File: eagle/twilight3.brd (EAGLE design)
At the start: 58 x 22 mm, 19 parts, among them IC1 TINY85, IC2 7805TV, Q1 IRF540

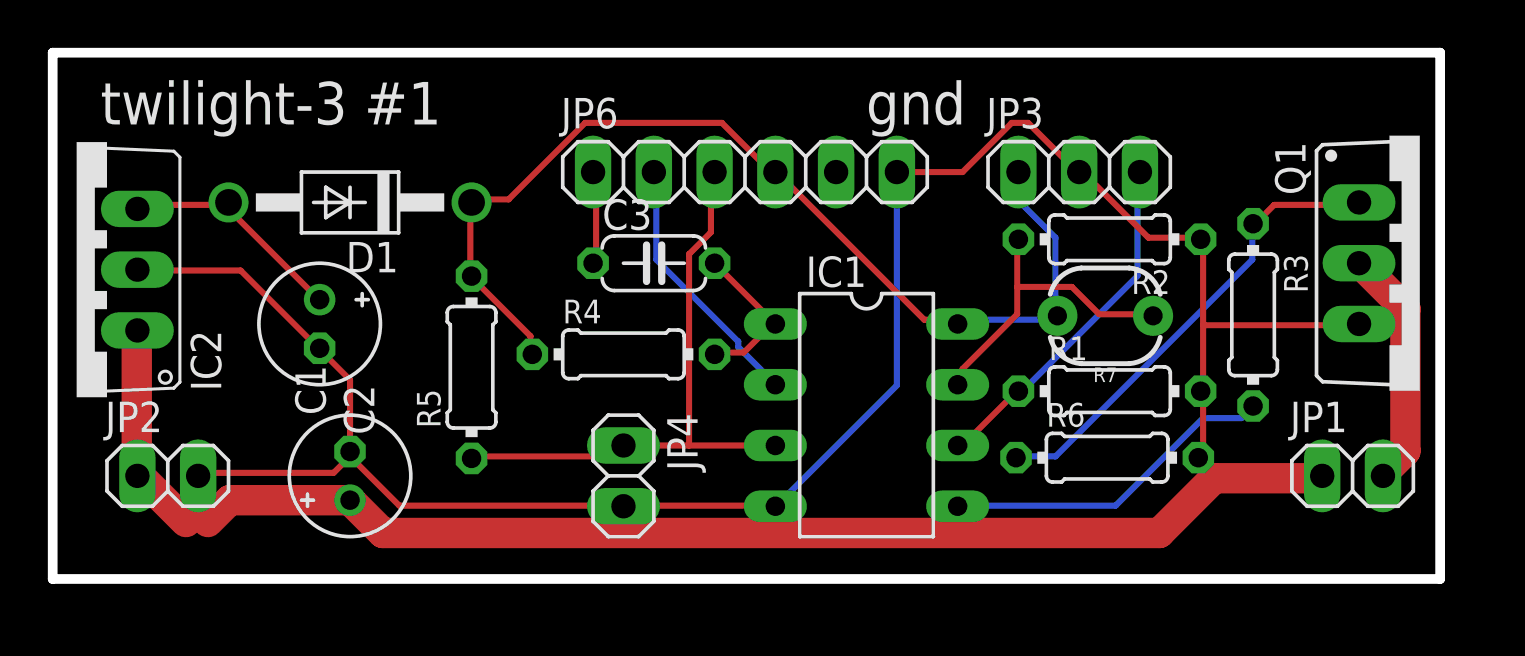
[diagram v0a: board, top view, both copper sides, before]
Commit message: fix issues #2, #3 and #4
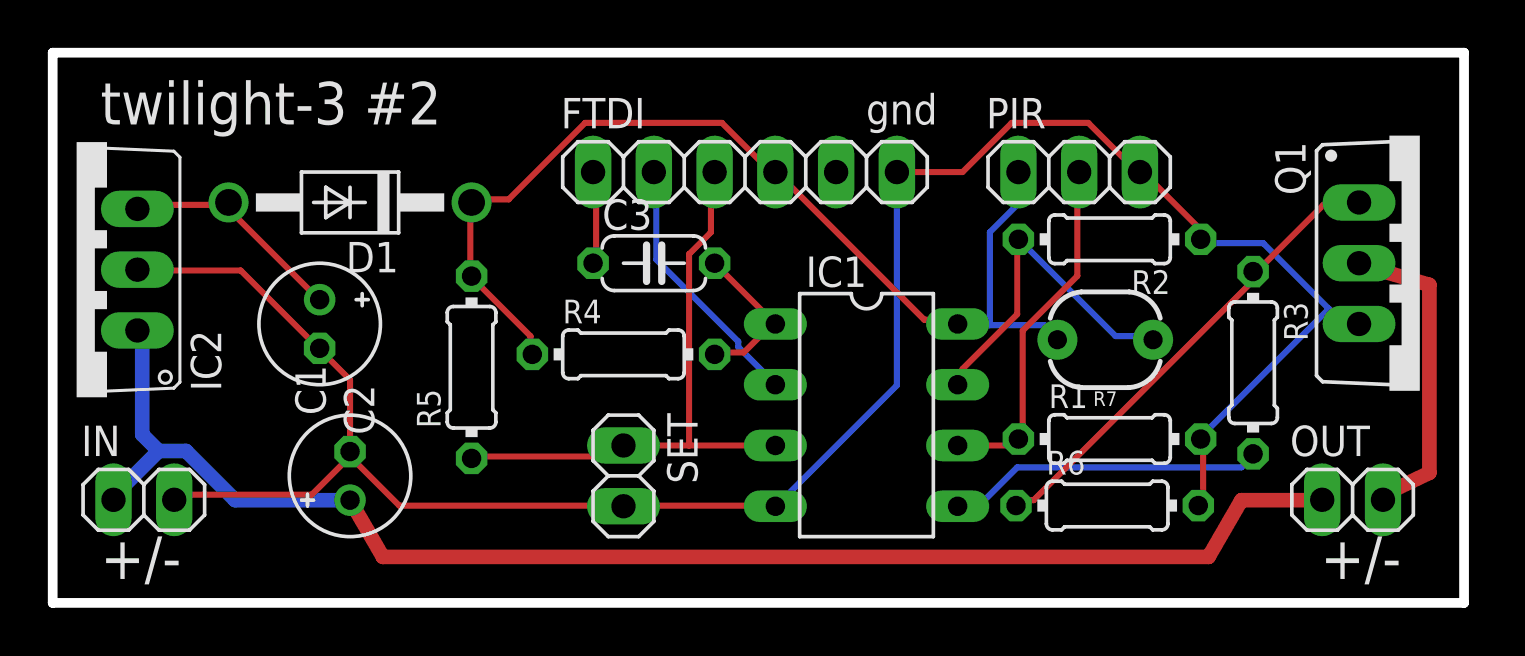
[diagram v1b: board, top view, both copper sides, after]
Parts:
- removed JP1: OUT, pinhead:1X02
- removed JP2: IN, pinhead:1X02
- added IN, OUT: (no value), pinhead:1X02
- FTDI: value PROG -> (none)
- PIR: value PIR -> (none)
- SET: value SET -> (none)
- moved R1 2.00 mm to (43.2, 68.8)
- moved R3 2.00 mm to (49.2, 72.0)
- moved R6 2.00 mm to (43.1, 66.1)
- moved R7 1.00 mm to (43.0, 73.0)
- renumbered JP3 to PIR, JP4 to SET, JP6 to FTDI
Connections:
- removed net SIG: IC1.6, PIR.3, R1.1
- new net N$9: IC1.6, PIR.2, R1.1
- net +12V: now also IN.1, OUT.1; no longer JP1.1, JP2.1
- net GND: now also IN.2, PIR.3; no longer JP2.2, PIR.2
- net GNDOUT: now also OUT.2; no longer JP1.2
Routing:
- net N$9: track 0.00 -> 14.9 mm
- net SIG: track 14.9 -> 0.00 mm
- net GND: track 86.9 -> 91.5 mm
- net GNDOUT: track 10.1 -> 13.3 mm
- net +12V: track 58.3 -> 60.6 mm
- net N$4: track 13.3 -> 14.5 mm
- net N$5: track 14.1 -> 13.3 mm
- removed copper zone on layer 16, net GND
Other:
- board size 58 x 22 mm -> 59 x 23 mm
- board text added: "(c) 2018 steve"
- board text added: "+/-"
- board text added: "twilight-3 #2"
- board text removed: "(c) 2017 steve"
- board text removed: "twilight-3 #1"
